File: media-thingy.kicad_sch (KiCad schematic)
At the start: 7 parts, among them J1 Conn_02x20_Odd_Even, J2 Conn_01x04, SW1 Switch, SW2 Switch, SW3 Switch, SW4 Switch, SW5 Switch

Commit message: correct header sizes
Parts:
- J1: footprint Connector_PinHeader_1.00mm:PinHeader_2x20_P1.00mm_Vertical -> Connector_PinSocket_2.54mm:PinSocket_2x20_P2.54mm_Vertical
- J2: footprint Connector_PinHeader_1.00mm:PinHeader_1x04_P1.00mm_Vertical -> Connector_PinSocket_2.54mm:PinSocket_1x04_P2.54mm_Vertical
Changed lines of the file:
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@@
 			)
 		)
-		(property "Footprint" "Connector_PinHeader_1.00mm:PinHeader_2x20_P1.00mm_Vertical"
+		(property "Footprint" "Connector_PinSocket_2.54mm:PinSocket_2x20_P2.54mm_Vertical"
 			(at 246.38 66.04 0)
 			(effects
@@
 			)
 		)
-		(property "Footprint" "Connector_PinHeader_1.00mm:PinHeader_1x04_P1.00mm_Vertical"
+		(property "Footprint" "Connector_PinSocket_2.54mm:PinSocket_1x04_P2.54mm_Vertical"
 			(at 248.92 105.41 0)
 			(effects

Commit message: complete pcb
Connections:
- net +5V: no longer J1.4 (Pin_4)
- net GPIO 16: no longer names the net of J1.36 (Pin_36)
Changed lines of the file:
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@@
-	(wire
-		(pts
-			(xy 267.97 45.72) (xy 254 45.72)
-		)
-		(stroke
-			(width 0)
-			(type default)
-		)
-	)
 	(wire
 		(pts
@@
 		)
 	)
-	(global_label "GPIO 16"
+	(global_label "GPIO 23"
 		(shape input)
-		(at 254 86.36 0)
+		(at 160.02 52.07 270)
 		(fields_autoplaced yes)
 		(effects
@@
 				(size 1.27 1.27)
 			)
-			(justify left)
+			(justify right)
 		)
 		(property "Intersheetrefs" "${INTERSHEET_REFS}"
-			(at 264.8471 86.36 0)
-			(effects
-				(font
-					(size 1.27 1.27)
-				)
-				(justify left)
-				(hide yes)
-			)
-		)
-	)
-	(global_label "GPIO 23"
+			(at 160.02 62.9171 90)
+			(effects
+				(font
+					(size 1.27 1.27)
+				)
+				(justify right)
+				(hide yes)
+			)
+		)
+	)
+	(global_label "LCD_DATA"
 		(shape input)
-		(at 160.02 52.07 270)
+		(at 241.3 45.72 180)
 		(fields_autoplaced yes)
 		(effects
@@
 		)
 		(property "Intersheetrefs" "${INTERSHEET_REFS}"
-			(at 160.02 62.9171 90)
+			(at 229.3643 45.72 0)
 			(effects
 				(font
@@
 	(global_label "LCD_DATA"
 		(shape input)
-		(at 241.3 45.72 180)
+		(at 243.84 107.95 180)
 		(fields_autoplaced yes)
 		(effects
@@
 		)
 		(property "Intersheetrefs" "${INTERSHEET_REFS}"
-			(at 229.3643 45.72 0)
+			(at 231.9043 107.95 0)
 			(effects
 				(font
@@
 		)
 	)
-	(global_label "LCD_DATA"
+	(global_label "GPIO 23"
 		(shape input)
-		(at 243.84 107.95 180)
+		(at 254 60.96 0)
 		(fields_autoplaced yes)
 		(effects
@@
 				(size 1.27 1.27)
 			)
-			(justify right)
+			(justify left)
 		)
 		(property "Intersheetrefs" "${INTERSHEET_REFS}"
-			(at 231.9043 107.95 0)
-			(effects
-				(font
-					(size 1.27 1.27)
-				)
-				(justify right)
-				(hide yes)
-			)
-		)
-	)
-	(global_label "GPIO 23"
+			(at 264.8471 60.96 0)
+			(effects
+				(font
+					(size 1.27 1.27)
+				)
+				(justify left)
+				(hide yes)
+			)
+		)
+	)
+	(global_label "LCD_CLK"
 		(shape input)
-		(at 254 60.96 0)
+		(at 243.84 110.49 180)
 		(fields_autoplaced yes)
 		(effects
@@
 				(size 1.27 1.27)
 			)
-			(justify left)
+			(justify right)
 		)
 		(property "Intersheetrefs" "${INTERSHEET_REFS}"
-			(at 264.8471 60.96 0)
-			(effects
-				(font
-					(size 1.27 1.27)
-				)
-				(justify left)
-				(hide yes)
-			)
-		)
-	)
-	(global_label "LCD_CLK"
+			(at 232.751 110.49 0)
+			(effects
+				(font
+					(size 1.27 1.27)
+				)
+				(justify right)
+				(hide yes)
+			)
+		)
+	)
+	(global_label "GPIO 22"
 		(shape input)
-		(at 243.84 110.49 180)
+		(at 140.97 52.07 270)
 		(fields_autoplaced yes)
 		(effects
@@
 		)
 		(property "Intersheetrefs" "${INTERSHEET_REFS}"
-			(at 232.751 110.49 0)
+			(at 140.97 62.9171 90)
 			(effects
 				(font
@@
 		)
 	)
-	(global_label "GPIO 22"
+	(global_label "GPIO 24"
 		(shape input)
-		(at 140.97 52.07 270)
+		(at 254 63.5 0)
 		(fields_autoplaced yes)
 		(effects
@@
 				(size 1.27 1.27)
 			)
-			(justify right)
+			(justify left)
 		)
 		(property "Intersheetrefs" "${INTERSHEET_REFS}"
-			(at 140.97 62.9171 90)
-			(effects
-				(font
-					(size 1.27 1.27)
-				)
-				(justify right)
-				(hide yes)
-			)
-		)
-	)
-	(global_label "GPIO 24"
+			(at 264.8471 63.5 0)
+			(effects
+				(font
+					(size 1.27 1.27)
+				)
+				(justify left)
+				(hide yes)
+			)
+		)
+	)
+	(global_label "LCD_CLK"
 		(shape input)
-		(at 254 63.5 0)
+		(at 241.3 48.26 180)
 		(fields_autoplaced yes)
 		(effects
@@
 				(size 1.27 1.27)
 			)
-			(justify left)
-		)
-		(property "Intersheetrefs" "${INTERSHEET_REFS}"
-			(at 264.8471 63.5 0)
-			(effects
-				(font
-					(size 1.27 1.27)
-				)
-				(justify left)
-				(hide yes)
-			)
-		)
-	)
-	(global_label "LCD_CLK"
-		(shape input)
-		(at 241.3 48.26 180)
-		(fields_autoplaced yes)
-		(effects
-			(font
-				(size 1.27 1.27)
-			)
 			(justify right)
 		)
@@
 					(unit 1)
 				)
-			)
-		)
-	)
-	(symbol
-		(lib_id "power:+5V")
-		(at 267.97 45.72 0)
-		(unit 1)
-		(exclude_from_sim no)
-		(in_bom yes)
-		(on_board yes)
-		(dnp no)
-		(fields_autoplaced yes)
-		(property "Reference" "#PWR015"
-			(at 267.97 49.53 0)
-			(effects
-				(font
-					(size 1.27 1.27)
-				)
-				(hide yes)
-			)
-		)
-		(property "Value" "+5V"
-			(at 267.97 40.64 0)
-			(effects
-				(font
-					(size 1.27 1.27)
-				)
-			)
-		)
-		(property "Footprint" ""
-			(at 267.97 45.72 0)
-			(effects
-				(font
-					(size 1.27 1.27)
-				)
-				(hide yes)
-			)
-		)
-		(property "Datasheet" ""
-			(at 267.97 45.72 0)
-			(effects
-				(font
-					(size 1.27 1.27)
-				)
-				(hide yes)
-			)
-		)
-		(property "Description" "Power symbol creates a global label with name \"+5V\""
-			(at 267.97 45.72 0)
-			(effects
-				(font
-					(size 1.27 1.27)
-				)
-				(hide yes)
-			)
-		)
-		(pin "1"
-		)
-		(instances
-			(project ""
-				(path "/e264615a-cfc9-4c30-a9bd-ca174a1b283c"
-					(reference "#PWR015")
-					(unit 1)
-				)

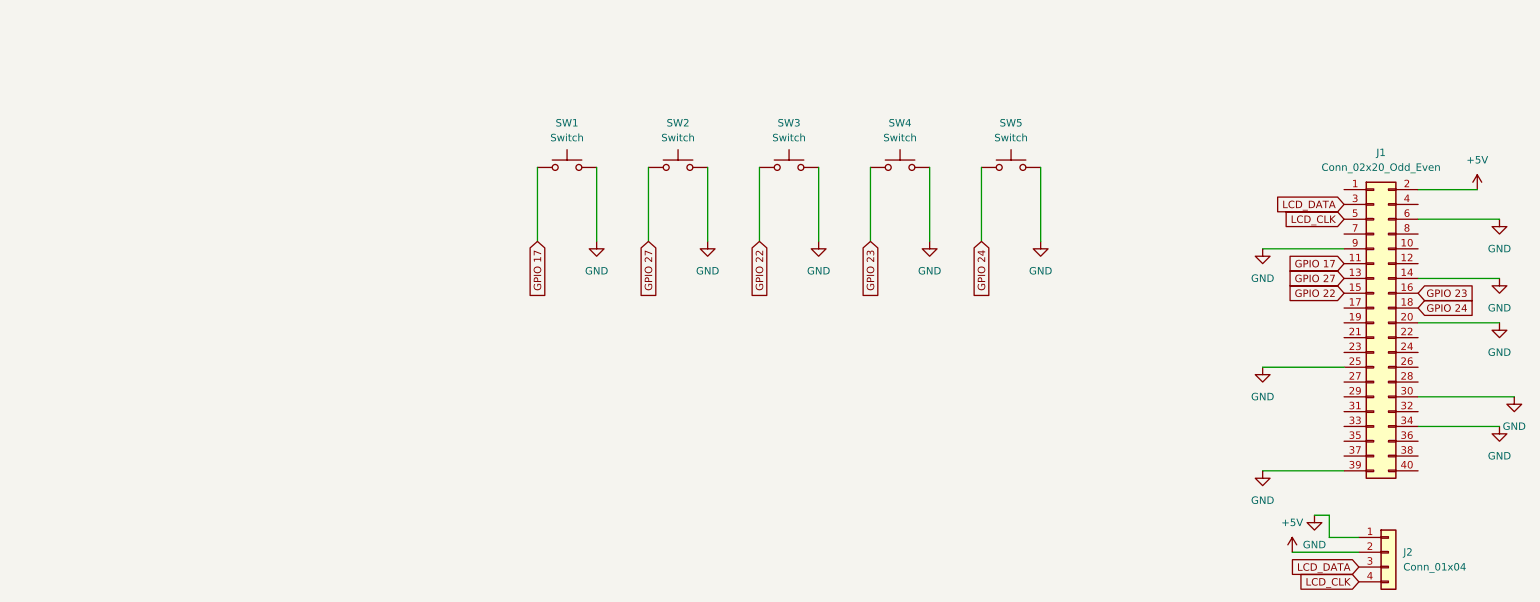
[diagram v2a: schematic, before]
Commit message: fix distance between switches and edge
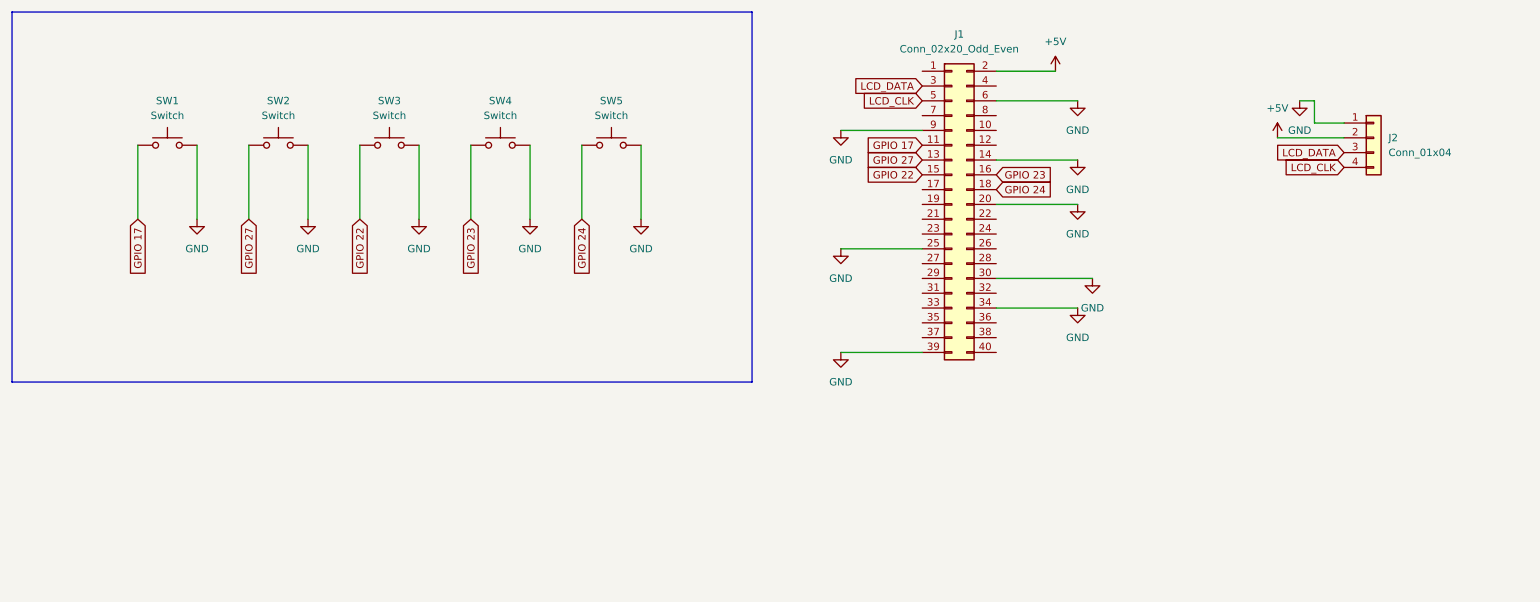
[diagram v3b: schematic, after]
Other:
- moved on the sheet: J1, J2, SW1, SW2, SW3, SW4, SW5
